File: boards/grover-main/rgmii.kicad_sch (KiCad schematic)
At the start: 60 parts

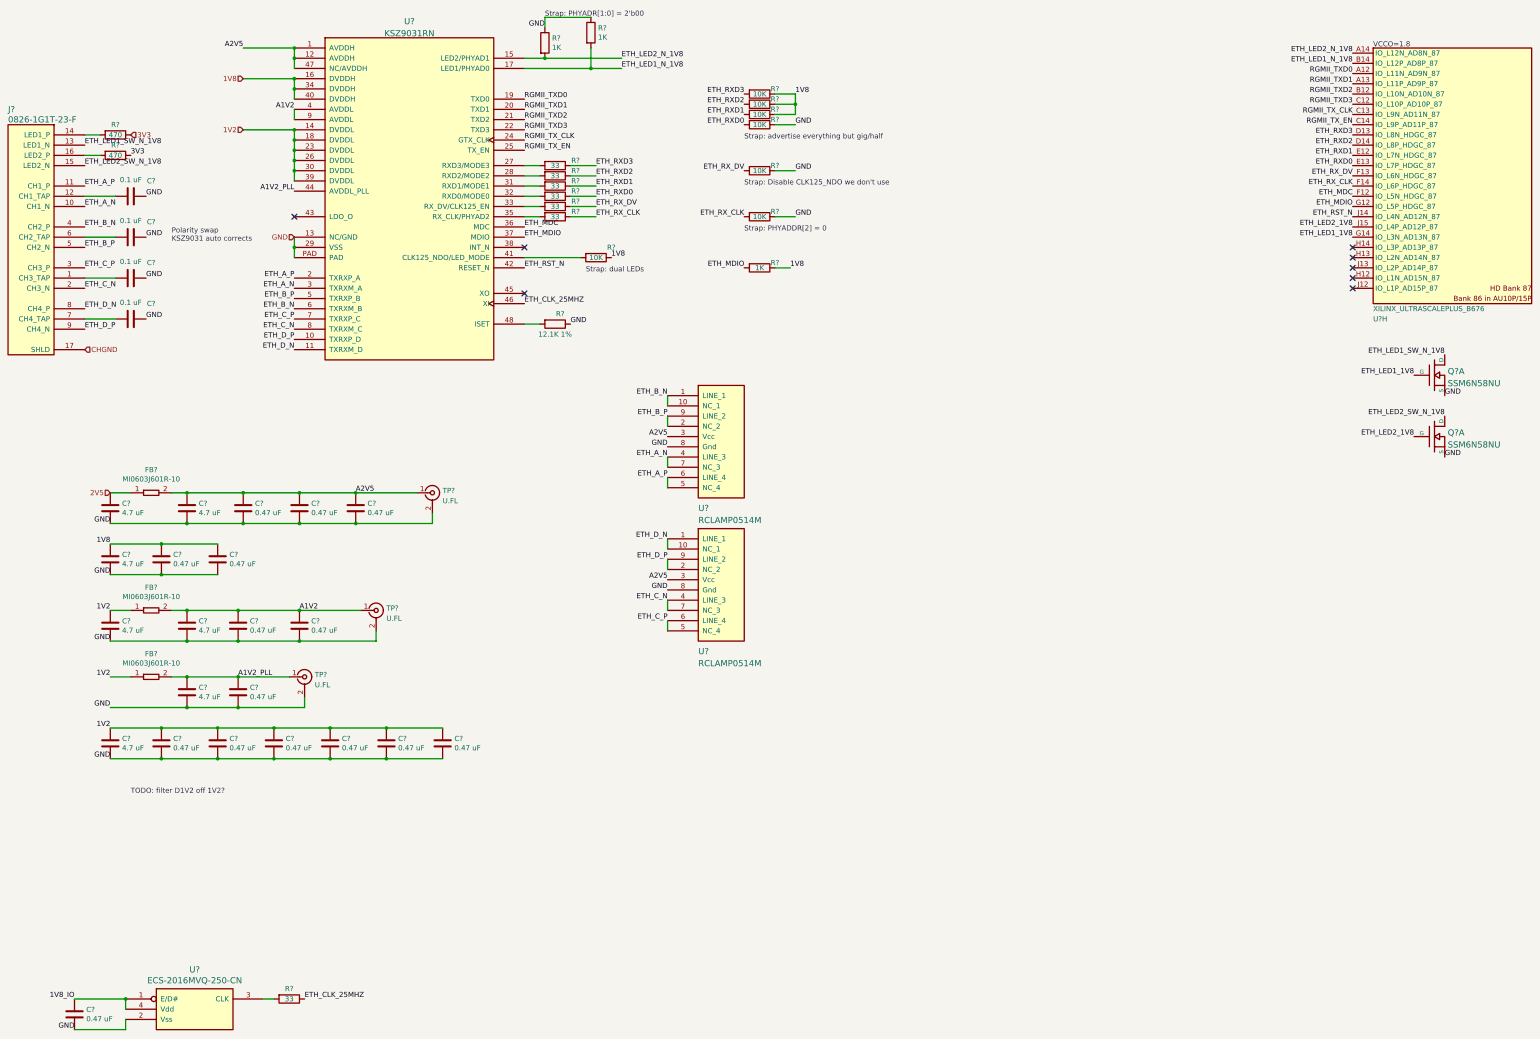
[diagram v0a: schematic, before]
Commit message: Continued initial schematic capture
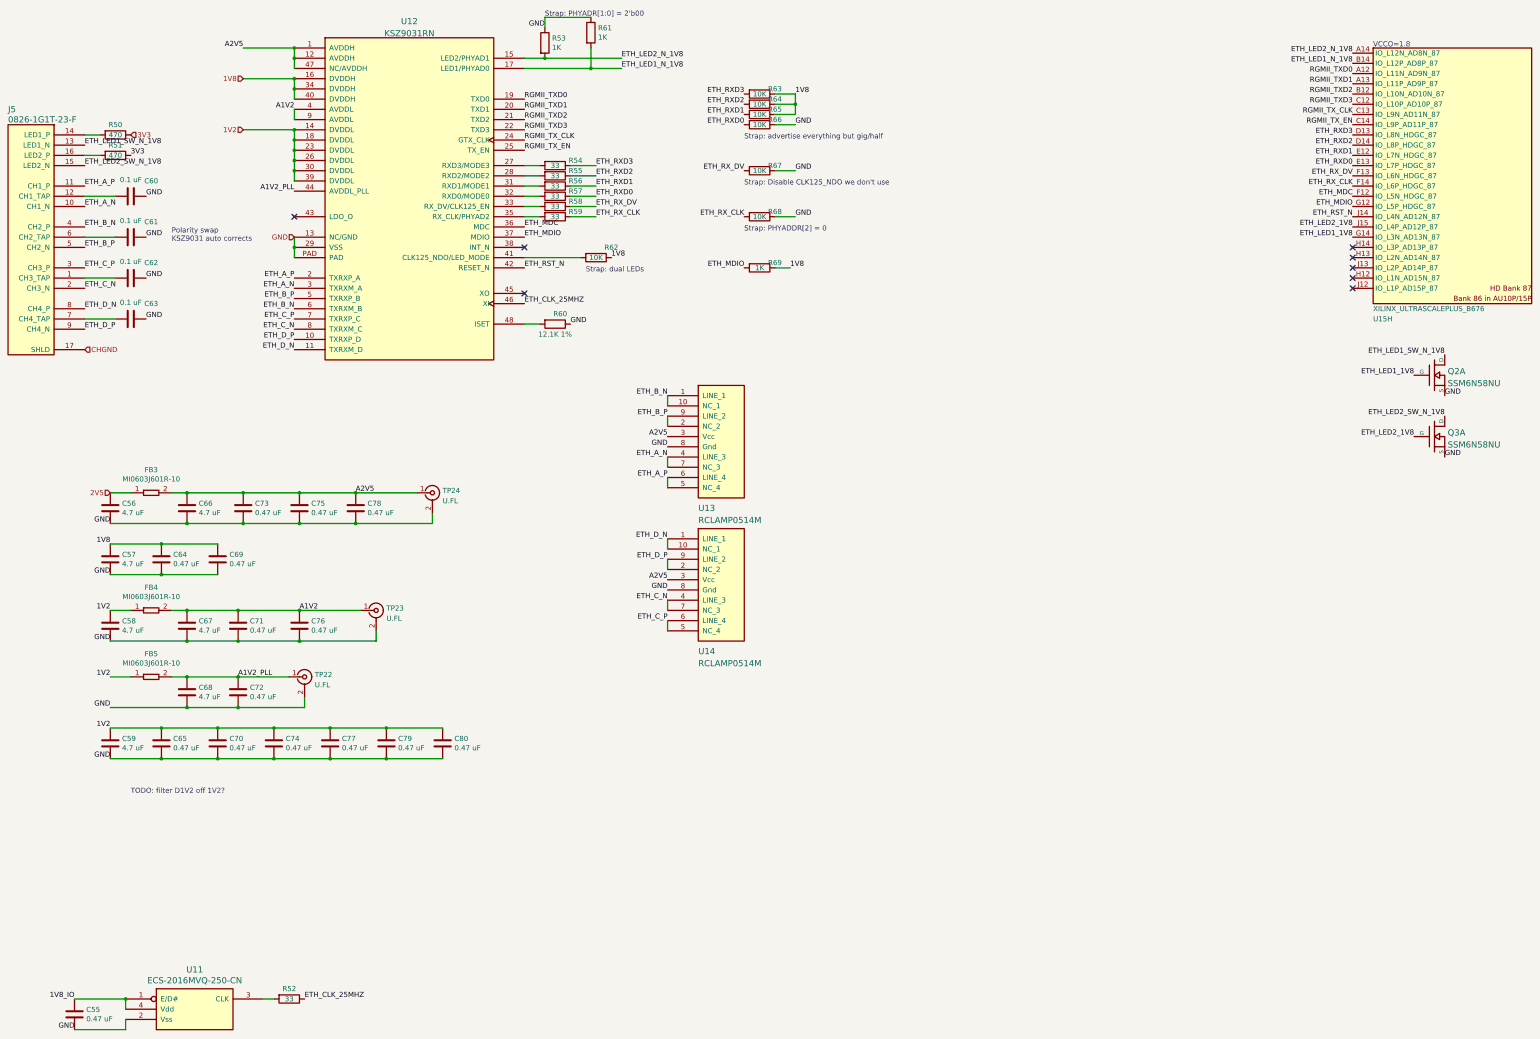
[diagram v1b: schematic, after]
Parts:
- gave numbers to parts that had none: 60
